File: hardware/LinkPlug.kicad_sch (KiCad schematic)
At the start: 4 parts, among them J1901 2x05_Horizontal, U1901 THVD24x2

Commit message: Update parts library
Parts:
- C1901: footprint Capacitor_SMD:C_0603_1608Metric -> V2_Capacitor_SMD:C_0603; symbol Device:C_Small -> V2_Device:C_0603_0u1; Mouser (none) -> 810-CGA3E2X7R1H104MA
- J1901: Mouser (none) -> 649-200211120001T4LF
- R1901: footprint Resistor_SMD:R_0603_1608Metric -> V2_Resistor_SMD:R_0603; symbol Device:R_Small -> V2_Device:R_0603_100R; Mouser (none) -> 71-CRCW0603100RFKEAH
- U1901: value THVD24x2 -> THVD2442; symbol V2_Interface_RS485:THVD24x2 -> V2_Interface_RS485:THVD2442; Mouser (none) -> 595-THVD2442DRCR
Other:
- moved on the sheet: C1901, J1901, R1901, U1901

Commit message: Update parts
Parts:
- C1901: Manufacturer (none) -> TDK; Product (none) -> CGA3E2X7R1H104M080AA
- J1901: Manufacturer (none) -> Amphenol FCI; Product (none) -> 20021112-00010T4LF
- R1901: Manufacturer (none) -> Vishay; Product (none) -> CRCW0603100RFKEAHP; Rating (none) -> 330mW
- U1901: Manufacturer (none) -> Texas Instruments; Mouser 595-THVD2442DRCR -> 595-THVD2442DRCR; Product (none) -> THVD2442DRCR
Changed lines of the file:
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@@
 			)
 		)
-		(property "Mouser" " 595-THVD2442DRCR "
+		(property "Mouser" "595-THVD2442DRCR"
+			(at 146.05 76.2 0)
+			(effects
+				(font
+					(size 1.27 1.27)
+				)
+				(hide yes)
+			)
+		)
+		(property "Product" "THVD2442DRCR "
+			(at 146.05 109.22 0)
+			(effects
+				(font
+					(size 1.27 1.27)
+				)
+				(hide yes)
+			)
+		)
+		(property "Manufacturer" "Texas Instruments"
+			(at 146.05 106.68 0)
+			(effects
+				(font
+					(size 1.27 1.27)
+				)
+				(hide yes)
+			)
+		)
+		(property "Sim.Enable" ""
 			(at 146.05 76.2 0)
 			(effects
@@
 			)
 		)
+		(property "Rating" "330mW"
+			(at 157.48 93.98 0)
+			(effects
+				(font
+					(size 1.27 1.27)
+				)
+				(hide yes)
+			)
+		)
+		(property "Manufacturer" "Vishay"
+			(at 157.48 88.9 0)
+			(effects
+				(font
+					(size 1.27 1.27)
+				)
+				(hide yes)
+			)
+		)
+		(property "Product" "CRCW0603100RFKEAHP"
+			(at 157.48 91.44 0)
+			(effects
+				(font
+					(size 1.27 1.27)
+				)
+				(hide yes)
+			)
+		)
+		(property "Sim.Enable" ""
+			(at 157.48 71.12 0)
+			(effects
+				(font
+					(size 1.27 1.27)
+				)
+				(hide yes)
+			)
+		)
 		(pin "1"
 		)
@@
 			)
 		)
+		(property "Manufacturer" "Amphenol FCI"
+			(at 147.32 149.86 0)
+			(effects
+				(font
+					(size 1.27 1.27)
+				)
+				(hide yes)
+			)
+		)
+		(property "Product" "20021112-00010T4LF"
+			(at 147.32 152.4 0)
+			(effects
+				(font
+					(size 1.27 1.27)
+				)
+				(hide yes)
+			)
+		)
+		(property "Sim.Enable" ""
+			(at 147.32 132.08 0)
+			(effects
+				(font
+					(size 1.27 1.27)
+				)
+				(hide yes)
+			)
+		)
 		(pin "1"
 		)
@@
 			(effects
 				(font
+					(size 1.27 1.27)
+				)
+				(hide yes)
+			)
+		)
+		(property "Manufacturer" "TDK"
+			(at 166.37 71.12 0)
+			(effects
+				(font
+					(size 1.27 1.27)
+				)
+				(hide yes)
+			)
+		)
+		(property "Product" "CGA3E2X7R1H104M080AA"
+			(at 166.37 73.66 0)
+			(effects
+				(font
+					(size 1.27 1.27)
+				)
+				(hide yes)
+			)
+		)
+		(property "Sim.Enable" ""
+			(at 166.37 55.88 0)
+			(effects
+				(font

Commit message: Refresh
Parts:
- C1901: Rating (none) -> 50V
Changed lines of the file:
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@@
 			)
 		)
-		(property "Description" "Power symbol creates a global label with name \"GND\" , ground"
+		(property "Description" ""
 			(at 166.37 58.42 0)
 			(effects
@@
 			)
 		)
-		(property "Sim.Enable" ""
-			(at 146.05 76.2 0)
-			(effects
-				(font
-					(size 1.27 1.27)
-				)
-				(hide yes)
-			)
-		)
 		(pin "1"
 		)
@@
 			)
 		)
-		(property "Sim.Enable" ""
-			(at 157.48 71.12 0)
-			(effects
-				(font
-					(size 1.27 1.27)
-				)
-				(hide yes)
-			)
-		)
 		(pin "1"
 		)
@@
 			)
 		)
-		(property "Sim.Enable" ""
-			(at 147.32 132.08 0)
-			(effects
-				(font
-					(size 1.27 1.27)
-				)
-				(hide yes)
-			)
-		)
 		(pin "1"
 		)
@@
 			)
 		)
-		(property "Description" "Power symbol creates a global label with name \"+5V\""
+		(property "Description" ""
 			(at 144.78 152.4 0)
 			(effects
@@
 			)
 		)
-		(property "Description" "Power symbol creates a global label with name \"GND\" , ground"
+		(property "Description" ""
 			(at 140.97 129.54 0)
 			(effects
@@
 			)
 		)
-		(property "Description" "Power symbol creates a global label with name \"+5V\""
+		(property "Description" ""
 			(at 140.97 134.62 0)
 			(effects
@@
 			)
 		)
-		(property "Description" "Power symbol creates a global label with name \"GND\" , ground"
+		(property "Description" ""
 			(at 146.05 91.44 0)
 			(effects
@@
 			)
 		)
-		(property "Description" "Power symbol creates a global label with name \"+5V\""
+		(property "Description" ""
 			(at 153.67 129.54 0)
 			(effects
@@
 			)
 		)
-		(property "Description" "Power symbol creates a global label with name \"+3V3\""
+		(property "Description" ""
 			(at 146.05 53.34 0)
 			(effects
@@
 			)
 		)
-		(property "Description" "Power symbol creates a global label with name \"GND\" , ground"
+		(property "Description" ""
 			(at 144.78 156.21 0)
 			(effects
@@
 			)
 		)
-		(property "Description" "Power symbol creates a global label with name \"GND\" , ground"
+		(property "Description" ""
 			(at 153.67 134.62 0)
 			(effects
@@
 			)
 		)
-		(property "Sim.Enable" ""
-			(at 166.37 55.88 0)
-			(effects
-				(font
+		(property "Rating" "50V"
+			(at 166.37 78.74 0)
+			(effects
+				(font

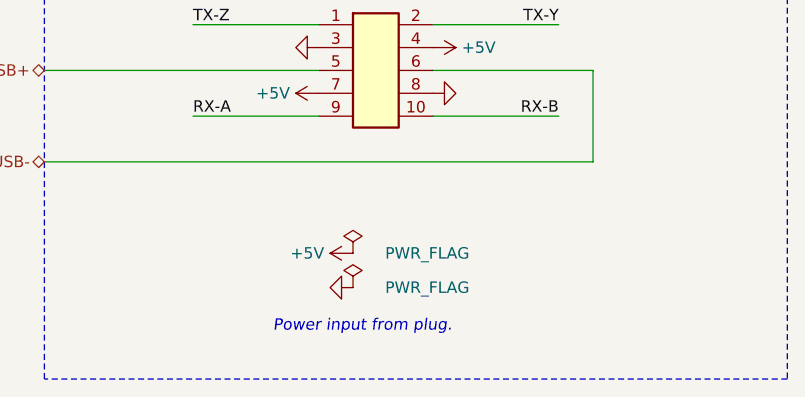
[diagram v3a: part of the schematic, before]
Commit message: Replace Order_Number
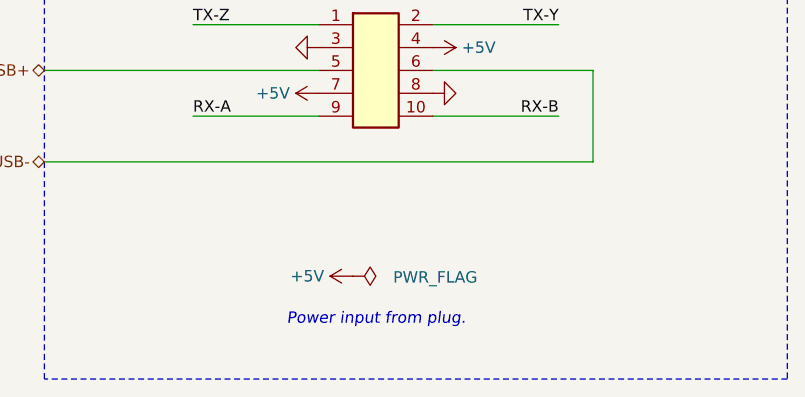
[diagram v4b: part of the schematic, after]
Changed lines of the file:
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@@
 	(title_block
 		(title "V2 Link")
-		(date "2025-10-27")
-		(rev "4")
+		(date "2026-02-10")
+		(rev "2026-02-10")
 		(company "Plug")
 	)
@@
 	(text "Power input from plug."
 		(exclude_from_sim no)
-		(at 135.89 161.29 0)
+		(at 137.414 160.528 0)
 		(effects
 			(font
@@
 	(symbol
 		(lib_id "V2_power:PWR_FLAG")
-		(at 144.78 156.21 270)
-		(unit 1)
-		(exclude_from_sim no)
-		(in_bom yes)
-		(on_board yes)
-		(dnp no)
-		(property "Reference" "#FLG01902"
-			(at 146.685 156.21 0)
-			(effects
-				(font
-					(size 1.27 1.27)
-				)
-				(hide yes)
-			)
-		)
-		(property "Value" "PWR_FLAG"
-			(at 153.035 156.21 90)
-			(effects
-				(font
-					(size 1.27 1.27)
-				)
-			)
-		)
-		(property "Footprint" ""
-			(at 144.78 156.21 0)
-			(effects
-				(font
-					(size 1.27 1.27)
-				)
-				(hide yes)
-			)
-		)
-		(property "Datasheet" ""
-			(at 144.78 156.21 0)
-			(effects
-				(font
-					(size 1.27 1.27)
-				)
-				(hide yes)
-			)
-		)
-		(property "Description" "Special symbol for telling ERC where power comes from"
-			(at 144.78 156.21 0)
-			(effects
-				(font
-					(size 1.27 1.27)
-				)
-				(hide yes)
-			)
-		)
-		(pin "1"
-		)
-		(instances
-			(project "pulse"
-				(path "/6c8448b4-b04d-47e1-934e-e40cbe27a7be/c6db2f80-f80f-4104-8ca1-02f0ab85cfea"
-					(reference "#FLG01902")
-					(unit 1)
-				)
-			)
-		)
-	)
-	(symbol
-		(lib_id "V2_power:PWR_FLAG")
-		(at 144.78 152.4 270)
+		(at 144.78 154.94 180)
 		(unit 1)
 		(exclude_from_sim no)
@@
 		(dnp no)
 		(property "Reference" "#FLG01901"
-			(at 146.685 152.4 0)
+			(at 144.78 156.845 0)
 			(effects
 				(font
@@
 		)
 		(property "Value" "PWR_FLAG"
-			(at 153.035 152.4 90)
+			(at 153.924 155.067 0)
 			(effects
 				(font
@@
 		)
 		(property "Footprint" ""
-			(at 144.78 152.4 0)
+			(at 144.78 154.94 0)
 			(effects
 				(font
@@
 		)
 		(property "Datasheet" ""
-			(at 144.78 152.4 0)
+			(at 144.78 154.94 0)
 			(effects
 				(font
@@
 		)
 		(property "Description" "Special symbol for telling ERC where power comes from"
-			(at 144.78 152.4 0)
+			(at 144.78 154.94 0)
 			(effects
 				(font
@@
 	(symbol
 		(lib_id "V2_power:+5V")
-		(at 144.78 152.4 90)
+		(at 144.78 154.94 90)
 		(unit 1)
 		(exclude_from_sim no)
@@
 		(dnp no)
 		(property "Reference" "#PWR01908"
-			(at 148.59 152.4 0)
+			(at 148.59 154.94 0)
 			(effects
 				(font
@@
 		)
 		(property "Value" "+5V"
-			(at 139.7 152.4 90)
+			(at 139.7 154.94 90)
 			(effects
 				(font
@@
 		)
 		(property "Footprint" ""
-			(at 144.78 152.4 0)
+			(at 144.78 154.94 0)
 			(effects
 				(font
@@
 		)
 		(property "Datasheet" ""
-			(at 144.78 152.4 0)
+			(at 144.78 154.94 0)
 			(effects
 				(font
@@
 		)
 		(property "Description" ""
-			(at 144.78 152.4 0)
+			(at 144.78 154.94 0)
 			(effects
 				(font
@@
 					(unit 1)
 				)
-			)
-		)
-	)
-	(symbol
-		(lib_id "V2_power:GND")
-		(at 144.78 156.21 270)
-		(unit 1)
-		(exclude_from_sim no)
-		(in_bom yes)
-		(on_board yes)
-		(dnp no)
-		(property "Reference" "#PWR01909"
-			(at 138.43 156.21 0)
-			(effects
-				(font
-					(size 1.27 1.27)
-				)
-				(hide yes)
-			)
-		)
-		(property "Value" "GND"
-			(at 139.7 156.21 90)
-			(effects
-				(font
-					(size 1.27 1.27)
-				)
-				(hide yes)
-			)
-		)
-		(property "Footprint" ""
-			(at 144.78 156.21 0)
-			(effects
-				(font
-					(size 1.27 1.27)
-				)
-				(hide yes)
-			)
-		)
-		(property "Datasheet" ""
-			(at 144.78 156.21 0)
-			(effects
-				(font
-					(size 1.27 1.27)
-				)
-				(hide yes)
-			)
-		)
-		(property "Description" ""
-			(at 144.78 156.21 0)
-			(effects
-				(font
-					(size 1.27 1.27)
-				)
-				(hide yes)
-			)
-		)
-		(pin "1"
-		)
-		(instances
-			(project "pulse"
-				(path "/6c8448b4-b04d-47e1-934e-e40cbe27a7be/c6db2f80-f80f-4104-8ca1-02f0ab85cfea"
-					(reference "#PWR01909")
-					(unit 1)
-				)

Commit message: Update Library
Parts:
- C1901: symbol V2_Device:C_0603_0u1 -> V2_Capacitor:0603_0u1
- R1901: symbol V2_Device:R_0603_100R -> V2_Resistor:0603_100R
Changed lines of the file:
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@@
 		(on_board yes)
 		(dnp no)
-		(property "Reference" "#PWR01902"
+		(property "Reference" "#PWR1902"
 			(at 166.37 64.77 0)
 			(effects
@@
 			(project "pulse"
 				(path "/6c8448b4-b04d-47e1-934e-e40cbe27a7be/c6db2f80-f80f-4104-8ca1-02f0ab85cfea"
-					(reference "#PWR01902")
+					(reference "#PWR1902")
 					(unit 1)
 				)
@@
 		(on_board yes)
 		(dnp no)
-		(property "Reference" "#FLG01901"
+		(property "Reference" "#FLG1901"
 			(at 144.78 156.845 0)
 			(effects
@@
 			(project "pulse"
 				(path "/6c8448b4-b04d-47e1-934e-e40cbe27a7be/c6db2f80-f80f-4104-8ca1-02f0ab85cfea"
-					(reference "#FLG01901")
+					(reference "#FLG1901")
 					(unit 1)
 				)
@@
 	)
 	(symbol
-		(lib_id "V2_Device:R_0603_100R")
+		(lib_id "V2_Resistor:0603_100R")
 		(at 157.48 71.12 0)
 		(unit 1)
@@
 		(on_board yes)
 		(dnp no)
-		(property "Reference" "#PWR01908"
+		(property "Reference" "#PWR1908"
 			(at 148.59 154.94 0)
 			(effects
@@
 			(project "pulse"
 				(path "/6c8448b4-b04d-47e1-934e-e40cbe27a7be/c6db2f80-f80f-4104-8ca1-02f0ab85cfea"
-					(reference "#PWR01908")
+					(reference "#PWR1908")
 					(unit 1)
 				)
@@
 		(on_board yes)
 		(dnp no)
-		(property "Reference" "#PWR01904"
+		(property "Reference" "#PWR1904"
 			(at 134.62 129.54 0)
 			(effects
@@
 			(project "pulse"
 				(path "/6c8448b4-b04d-47e1-934e-e40cbe27a7be/c6db2f80-f80f-4104-8ca1-02f0ab85cfea"
-					(reference "#PWR01904")
+					(reference "#PWR1904")
 					(unit 1)
 				)
@@
 		(on_board yes)
 		(dnp no)
-		(property "Reference" "#PWR01906"
+		(property "Reference" "#PWR1906"
 			(at 144.78 134.62 0)
 			(effects
@@
 			(project "pulse"
 				(path "/6c8448b4-b04d-47e1-934e-e40cbe27a7be/c6db2f80-f80f-4104-8ca1-02f0ab85cfea"
-					(reference "#PWR01906")
+					(reference "#PWR1906")
 					(unit 1)
 				)
@@
 		(on_board yes)
 		(dnp no)
-		(property "Reference" "#PWR01903"
+		(property "Reference" "#PWR1903"
 			(at 146.05 97.79 0)
 			(effects
@@
 			(project "pulse"
 				(path "/6c8448b4-b04d-47e1-934e-e40cbe27a7be/c6db2f80-f80f-4104-8ca1-02f0ab85cfea"
-					(reference "#PWR01903")
+					(reference "#PWR1903")
 					(unit 1)
 				)
@@
 		(on_board yes)
 		(dnp no)
-		(property "Reference" "#PWR01905"
+		(property "Reference" "#PWR1905"
 			(at 149.86 129.54 0)
 			(effects
@@
 			(project "pulse"
 				(path "/6c8448b4-b04d-47e1-934e-e40cbe27a7be/c6db2f80-f80f-4104-8ca1-02f0ab85cfea"
-					(reference "#PWR01905")
+					(reference "#PWR1905")
 					(unit 1)
 				)
@@
 		(on_board yes)
 		(dnp no)
-		(property "Reference" "#PWR01901"
+		(property "Reference" "#PWR1901"
 			(at 146.05 57.15 0)
 			(effects
@@
 			(project "pulse"
 				(path "/6c8448b4-b04d-47e1-934e-e40cbe27a7be/c6db2f80-f80f-4104-8ca1-02f0ab85cfea"
-					(reference "#PWR01901")
+					(reference "#PWR1901")
 					(unit 1)
 				)
@@
 		(on_board yes)
 		(dnp no)
-		(property "Reference" "#PWR01907"
+		(property "Reference" "#PWR1907"
 			(at 160.02 134.62 0)
 			(effects
@@
 			(project "pulse"
 				(path "/6c8448b4-b04d-47e1-934e-e40cbe27a7be/c6db2f80-f80f-4104-8ca1-02f0ab85cfea"
-					(reference "#PWR01907")
-					(unit 1)
-				)
-			)
-		)
-	)
-	(symbol
-		(lib_id "V2_Device:C_0603_0u1")
+					(reference "#PWR1907")
+					(unit 1)
+				)
+			)
+		)
+	)
+	(symbol
+		(lib_id "V2_Capacitor:0603_0u1")
 		(at 166.37 55.88 0)
 		(unit 1)

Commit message: Update
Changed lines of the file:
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@@
 		)
 		(property "Value" "+5V"
-			(at 139.7 154.94 90)
-			(effects
-				(font
-					(size 1.27 1.27)
+			(at 138.43 154.94 90)
+			(effects
+				(font
+					(size 1.27 1.27)
+					(color 255 92 187 1)
 				)
 			)
@@
 				(font
 					(size 1.27 1.27)
+					(color 255 92 187 1)
 				)
 			)
@@
 				(font
 					(size 1.27 1.27)
+					(color 255 92 187 1)
 				)
 			)
@@
 				(font
 					(size 1.27 1.27)
-				)
-			)
+					(color 255 92 187 1)
+				)
+			)

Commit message: KiCad 10
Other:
- company: Plug -> Versio Duo
